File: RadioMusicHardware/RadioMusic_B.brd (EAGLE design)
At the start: 107 x 19.5 mm, 46 parts, among them IC1 REG1117, IC4 TL074, SW1 KMR2, X2 32.768, X3 microUSB

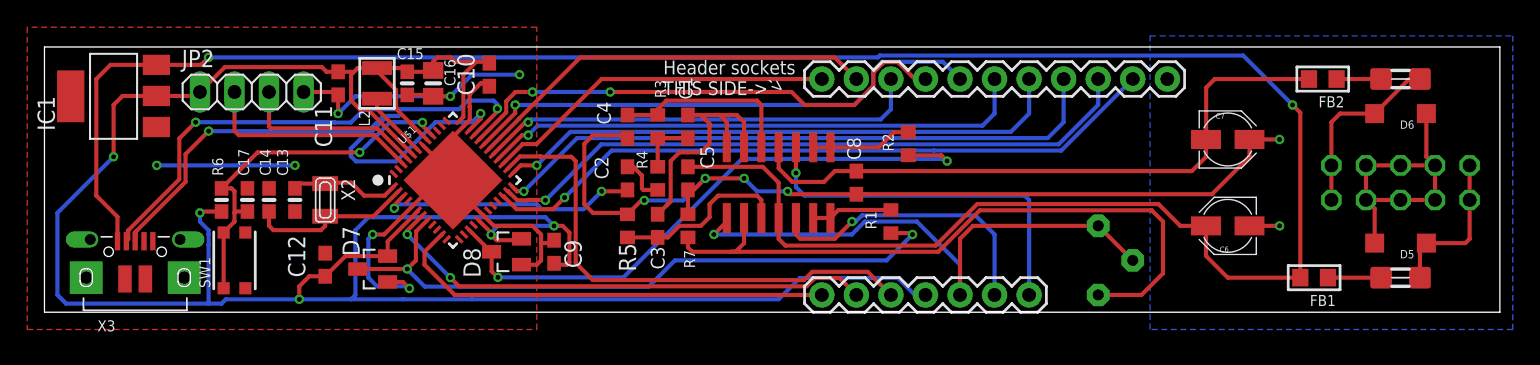
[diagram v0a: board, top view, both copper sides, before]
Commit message: Connect DGND/GND via inductor. Tidy silking.
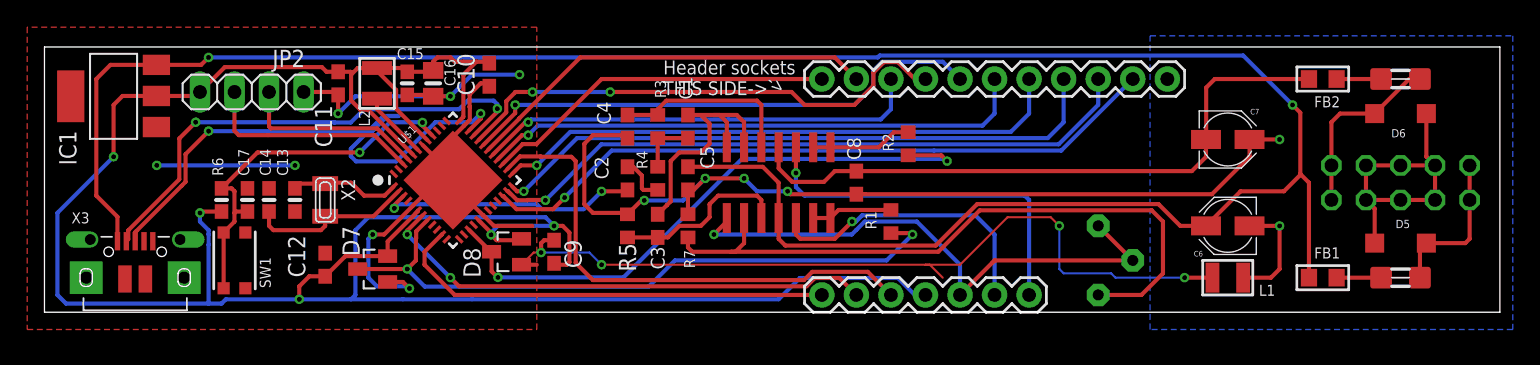
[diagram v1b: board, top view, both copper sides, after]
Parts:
- added L1: 10uH, microbuilder:INDUCTOR_1007
- moved FB1 0.64 mm to (94.0, 2.54)
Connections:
- net DGND: now also L1.P$2
- net GND: now also L1.P$1
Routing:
- net DGND: track 63.1 -> 119.3 mm, vias 7 -> 11
- net GND: track 91.9 -> 98.0 mm
- net +12V: track 170.3 -> 169.3 mm
- net AUDIO_OUT: track 41.9 -> 41.0 mm
- net N$22: track 3.91 -> 3.27 mm

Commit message: Rev A of MTM Brain board.
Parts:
- removed U$1: ATSAMD51G19A, SparkFun-IC-Microcontroller:QFN-48
- removed X3: microUSB, microbuilder:4UCONN_20329_V2
- added J1: UJ2-MIBH2-4-SMT-TR, UJ2-MIBH2-4-SMT-TR:CUI_UJ2-MIBH2-4-SMT-TR
- added U1: ATSAMD51G19A, SparkFun-IC-Microcontroller:QFN-48
- C10, C11, C12, C9: device adafruit:C0603 -> rcl:C0603
- C16: value 10uF -> 10u
- C17: value 1uF -> 1u
- D5, D6: value 1N4001 -> S1M; device diode:SOD123 -> diode:SMA
- moved F1 0.95 mm to (99.7, 1.59)
- moved F2 0.64 mm to (99.7, 17.8)
- moved D6 0.45 mm to (99.4, 14.3)
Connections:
- net !RESET: now also U1.40; no longer U$1.40
- net +12V: now also J1.1; no longer X3.VBUS
- net 3V3: now also U1.17, U1.36, U1.41, U1.44, U1.6; no longer U$1.17, U$1.36, U$1.41, U$1.44, U$1.6
- net CHANNEL_POT: now also U1.11; no longer U$1.11
- net D+: now also J1.3, U1.34; no longer U$1.34, X3.D+
- net D-: now also J1.2, U1.33; no longer U$1.33, X3.D-
- net DAC: now also U1.3; no longer U$1.3
- net DGND: now also J1.5, J1.SH1, J1.SH2, J1.SH3, J1.SH4, J1.SH5, U1.18, U1.35, U1.42, U1.5, U1.EP; no longer U$1.18, U$1.35, U$1.42, U$1.5, U$1.EP, X3.BASE@1, X3.BASE@2, X3.GND, X3.SPRT@1, X3.SPRT@2, X3.SPRT@3, X3.SPRT@4
- net LED1: now also U1.22; no longer U$1.22
- net LED2: now also U1.23; no longer U$1.23
- net LED3: now also U1.24; no longer U$1.24
- net LED4: now also U1.25; no longer U$1.25
- net LED_RESET: now also U1.30; no longer U$1.30
- net MISO: now also U1.27; no longer U$1.27
- net MOSI: now also U1.28; no longer U$1.28
- net N$11: now also U1.43; no longer U$1.43
- net N$13: now also U1.39; no longer U$1.39
- net N$8: now also U1.1; no longer U$1.1
- net N$9: now also U1.2; no longer U$1.2
- net PIN20/A6: now also U1.15; no longer U$1.15
- net PIN22/A8: now also U1.8; no longer U$1.8
- net RESET_CV: now also U1.32; no longer U$1.32
- net RESET_SW: now also U1.31; no longer U$1.31
- net SCLK: now also U1.26; no longer U$1.26
- net SS: now also U1.29; no longer U$1.29
- net SWCLK: now also U1.45; no longer U$1.45
- net SWDIO: now also U1.46; no longer U$1.46
- net TIME_POT: now also U1.7; no longer U$1.7
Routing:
- net DGND: track 119.3 -> 128.4 mm
- net -12V_INLET: track 13.5 -> 15.1 mm
- net +12V_INLET: track 11.4 -> 12.3 mm
- net 3V3: track 187.4 -> 186.8 mm
- net D-: track 36.8 -> 37.4 mm
- net D+: track 42.6 -> 43.2 mm
- net +12V: track 169.3 -> 169.9 mm
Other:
- board text added: "3V3"
- board text added: "CLK"
- board text added: "Dec 2014 / Summer 2019 musicthing.co.uk CC-BY-SA"
- board text added: "GND"
- board text added: "HEADERS ->"
- board text added: "IO"
- board text added: "Inspired by: John Cage Don Buchla Akin Fernandez Stockhausen Nicholas Collins Max Neuhaus UbuWeb Resonance FM John Peel archive.org"
- board text added: "MTM Brain PCB Rev A Designed in London Tom Whitwell, Tom Armitage"
- board text added: "Thanks to: Paul Stoffregen, Steven Thonk, The Muff Wigglers Limor Fried, Albert van Dalen"
- board text removed: "<-AUDIO OUT"
- board text removed: "December 2014 musicthing.co.uk CC-BY-SA"
- board text removed: "Header sockets THIS SIDE->"
- board text removed: "Inspired by: John Cage Don Buchla Akin Fernandez Stockhausen Nicholas Collins Max Neuhaus UbuWeb Resonance FM John Peel archive.org Thanks to: Paul Stoffregen, Steven Thonk, The Muff Wigglers"
- board text removed: "Radio Music Back PCB Rev2 Designed in Herne Hill, London by Tom Whitwell"
- board text removed: "TEENSY 3.1"
- board text removed: "USB this end"
